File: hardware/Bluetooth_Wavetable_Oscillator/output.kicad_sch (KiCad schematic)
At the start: 14 parts, among them J2 AudioJack2, U6 NE5532

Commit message: add audio test files
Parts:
- C13, C14, C17, C18, C19: footprint (none) -> Capacitor_THT:C_Disc_D5.0mm_W2.5mm_P5.00mm
- C16: footprint (none) -> Capacitor_THT:CP_Radial_D5.0mm_P2.50mm
- R1, R2, R3, R4, R5: footprint (none) -> Resistor_THT:R_Axial_DIN0204_L3.6mm_D1.6mm_P7.62mm_Horizontal
- RV1: footprint (none) -> Trimmer-potentiometer:Trimmer-potentiometer
- U6: footprint (none) -> Package_DIP:DIP-8_W7.62mm
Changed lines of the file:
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@@
 			)
 		)
-		(property "Footprint" ""
+		(property "Footprint" "Resistor_THT:R_Axial_DIN0204_L3.6mm_D1.6mm_P7.62mm_Horizontal"
 			(at 168.91 99.568 90)
 			(effects
@@
 			)
 		)
-		(property "Footprint" ""
+		(property "Footprint" "Resistor_THT:R_Axial_DIN0204_L3.6mm_D1.6mm_P7.62mm_Horizontal"
 			(at 190.5 114.808 90)
 			(effects
@@
 			)
 		)
-		(property "Footprint" ""
+		(property "Footprint" "Capacitor_THT:CP_Radial_D5.0mm_P2.50mm"
 			(at 143.51 96.8248 0)
 			(effects
@@
 			)
 		)
-		(property "Footprint" ""
+		(property "Footprint" "Capacitor_THT:C_Disc_D5.0mm_W2.5mm_P5.00mm"
 			(at 159.7152 116.84 0)
 			(effects
@@
 			)
 		)
-		(property "Footprint" ""
+		(property "Footprint" "Resistor_THT:R_Axial_DIN0204_L3.6mm_D1.6mm_P7.62mm_Horizontal"
 			(at 78.74 97.028 90)
 			(effects
@@
 			)
 		)
-		(property "Footprint" ""
+		(property "Footprint" "Package_DIP:DIP-8_W7.62mm"
 			(at 189.23 99.06 0)
 			(effects
@@
 			)
 		)
-		(property "Footprint" ""
+		(property "Footprint" "Capacitor_THT:C_Disc_D5.0mm_W2.5mm_P5.00mm"
 			(at 104.14 83.5152 0)
 			(effects
@@
 			)
 		)
-		(property "Footprint" ""
+		(property "Footprint" "Package_DIP:DIP-8_W7.62mm"
 			(at 118.11 97.79 0)
 			(effects
@@
 			)
 		)
-		(property "Footprint" ""
+		(property "Footprint" "Capacitor_THT:C_Disc_D5.0mm_W2.5mm_P5.00mm"
 			(at 138.1252 179.07 0)
 			(effects
@@
 			)
 		)
-		(property "Footprint" ""
+		(property "Footprint" "Resistor_THT:R_Axial_DIN0204_L3.6mm_D1.6mm_P7.62mm_Horizontal"
 			(at 168.91 107.188 90)
 			(effects
@@
 			)
 		)
-		(property "Footprint" ""
+		(property "Footprint" "Package_DIP:DIP-8_W7.62mm"
 			(at 127 166.37 0)
 			(effects
@@
 			)
 		)
-		(property "Footprint" ""
+		(property "Footprint" "Capacitor_THT:C_Disc_D5.0mm_W2.5mm_P5.00mm"
 			(at 102.5652 106.68 0)
 			(effects
@@
 			)
 		)
-		(property "Footprint" ""
+		(property "Footprint" "Resistor_THT:R_Axial_DIN0204_L3.6mm_D1.6mm_P7.62mm_Horizontal"
 			(at 95.25 97.028 90)
 			(effects
@@
 			)
 		)
-		(property "Footprint" ""
+		(property "Footprint" "Trimmer-potentiometer:Trimmer-potentiometer"
 			(at 55.88 171.45 0)
 			(effects
@@
 			)
 		)
-		(property "Footprint" ""
+		(property "Footprint" "Capacitor_THT:C_Disc_D5.0mm_W2.5mm_P5.00mm"
 			(at 117.8052 179.07 0)
 			(effects

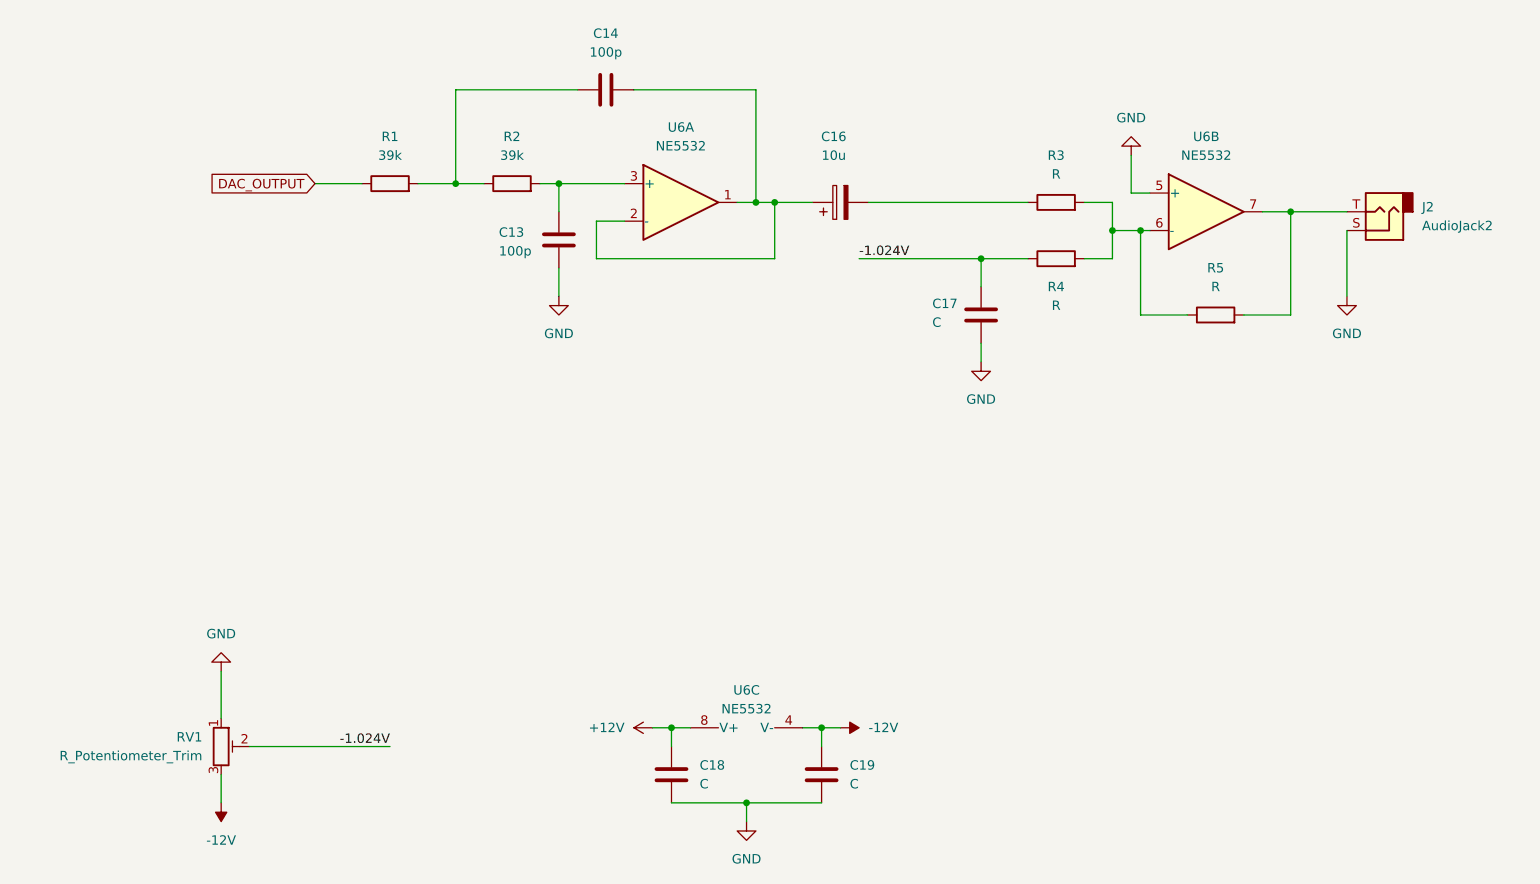
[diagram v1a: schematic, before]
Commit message: add bth components, add component values, update SPI pins, change disp power supply to 5V
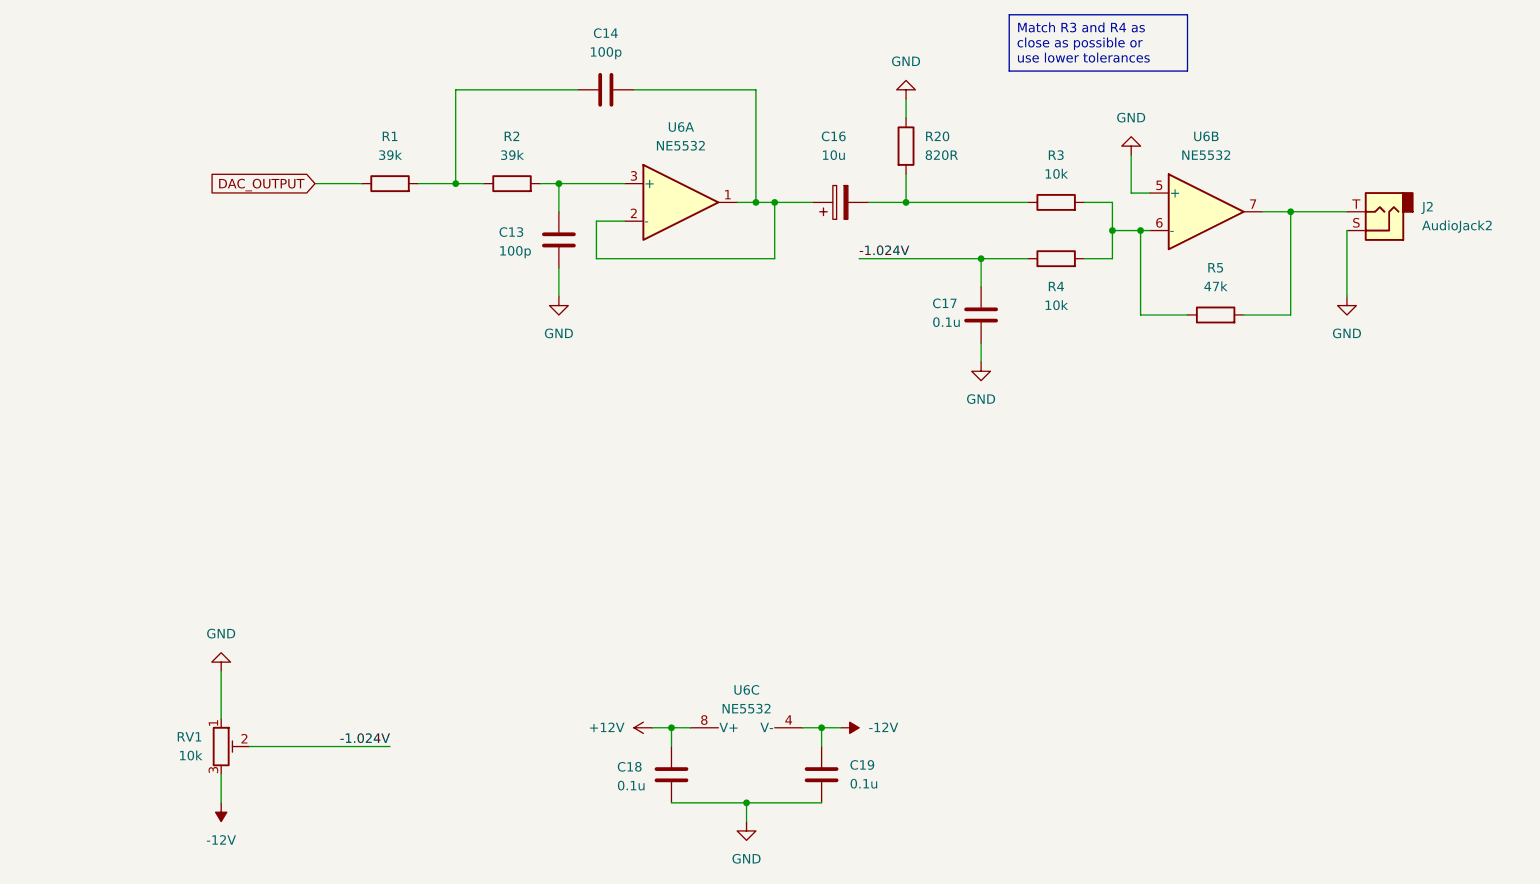
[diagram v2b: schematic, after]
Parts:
- added R20: 820R, symbol Device:R
- C17, C18, C19: value C -> 0.1u
- R3, R4: value R -> 10k
- R5: value R -> 47k
- RV1: value R_Potentiometer_Trim -> 10k
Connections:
- net GND: now also R20.1
- net at C16.2, R3.1: now also R20.2
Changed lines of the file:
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@@
+	)
+	(junction
+		(at 148.59 97.79)
+		(diameter 0)
+		(color 0 0 0 0)
 	)
 	(junction
@@
 	(wire
 		(pts
+			(xy 148.59 93.98) (xy 148.59 97.79)
+		)
+		(stroke
+			(width 0)
+			(type default)
+		)
+	)
+	(wire
+		(pts
 			(xy 142.24 105.41) (xy 158.75 105.41)
 		)
@@
 	(wire
 		(pts
-			(xy 143.51 97.79) (xy 165.1 97.79)
+			(xy 143.51 97.79) (xy 148.59 97.79)
 		)
 		(stroke
@@
 	(wire
 		(pts
+			(xy 148.59 83.82) (xy 148.59 86.36)
+		)
+		(stroke
+			(width 0)
+			(type default)
+		)
+	)
+	(wire
+		(pts
 			(xy 128.27 97.79) (xy 125.73 97.79)
 		)
@@
 	(wire
 		(pts
+			(xy 148.59 97.79) (xy 165.1 97.79)
+		)
+		(stroke
+			(width 0)
+			(type default)
+		)
+	)
+	(wire
+		(pts
 			(xy 130.81 97.79) (xy 128.27 97.79)
 		)
@@
 		)
 	)
-	(label "-1.024V"
-		(at 142.24 105.41 0)
-		(fields_autoplaced yes)
+	(text_box "Match R3 and R4 as close as possible or use lower tolerances"
+		(exclude_from_sim no)
+		(at 162.56 72.39 0)
+		(size 24.13 7.62)
+		(stroke
+			(width 0)
+			(type default)
+		)
+		(fill
+			(type none)
+		)
 		(effects
 			(font
 				(size 1.27 1.27)
 			)
-			(justify left bottom)
+			(justify left top)
 		)
 	)
 	(label "-1.024V"
-		(at 78.74 171.45 180)
+		(at 142.24 105.41 0)
 		(fields_autoplaced yes)
 		(effects
@@
 				(size 1.27 1.27)
 			)
+			(justify left bottom)
+		)
+	)
+	(label "-1.024V"
+		(at 78.74 171.45 180)
+		(fields_autoplaced yes)
+		(effects
+			(font
+				(size 1.27 1.27)
+			)
 			(justify right bottom)
 		)
@@
 			)
 		)
-		(property "Value" "R"
+		(property "Value" "10k"
 			(at 168.91 93.98 90)
 			(effects
@@
 	)
 	(symbol
+		(lib_id "power:GND")
+		(at 148.59 83.82 180)
+		(unit 1)
+		(exclude_from_sim no)
+		(in_bom yes)
+		(on_board yes)
+		(dnp no)
+		(fields_autoplaced yes)
+		(property "Reference" "#PWR051"
+			(at 148.59 77.47 0)
+			(effects
+				(font
+					(size 1.27 1.27)
+				)
+				(hide yes)
+			)
+		)
+		(property "Value" "GND"
+			(at 148.59 78.74 0)
+			(effects
+				(font
+					(size 1.27 1.27)
+				)
+			)
+		)
+		(property "Footprint" ""
+			(at 148.59 83.82 0)
+			(effects
+				(font
+					(size 1.27 1.27)
+				)
+				(hide yes)
+			)
+		)
+		(property "Datasheet" ""
+			(at 148.59 83.82 0)
+			(effects
+				(font
+					(size 1.27 1.27)
+				)
+				(hide yes)
+			)
+		)
+		(property "Description" "Power symbol creates a global label with name \"GND\" , ground"
+			(at 148.59 83.82 0)
+			(effects
+				(font
+					(size 1.27 1.27)
+				)
+				(hide yes)
+			)
+		)
+		(pin "1"
+		)
+		(instances
+			(project ""
+				(path "/fda99055-d953-4203-b673-64a5e6540552/e721cc72-9f0b-4653-9ded-ede3b48f082c"
+					(reference "#PWR051")
+					(unit 1)
+				)
+			)
+		)
+	)
+	(symbol
 		(lib_id "Device:R")
 		(at 190.5 113.03 90)
@@
 			)
 		)
-		(property "Value" "R"
+		(property "Value" "47k"
 			(at 190.5 109.22 90)
 			(effects
@@
 			)
 		)
-		(property "Value" "C"
+		(property "Value" "0.1u"
 			(at 152.146 114.046 0)
 			(effects
@@
 	)
 	(symbol
+		(lib_id "Device:R")
+		(at 148.59 90.17 0)
+		(unit 1)
+		(exclude_from_sim no)
+		(in_bom yes)
+		(on_board yes)
+		(dnp no)
+		(fields_autoplaced yes)
+		(property "Reference" "R20"
+			(at 151.13 88.8999 0)
+			(effects
+				(font
+					(size 1.27 1.27)
+				)
+				(justify left)
+			)
+		)
+		(property "Value" "820R"
+			(at 151.13 91.4399 0)
+			(effects
+				(font
+					(size 1.27 1.27)
+				)
+				(justify left)
+			)
+		)
+		(property "Footprint" ""
+			(at 146.812 90.17 90)
+			(effects
+				(font
+					(size 1.27 1.27)
+				)
+				(hide yes)
+			)
+		)
+		(property "Datasheet" "~"
+			(at 148.59 90.17 0)
+			(effects
+				(font
+					(size 1.27 1.27)
+				)
+				(hide yes)
+			)
+		)
+		(property "Description" "Resistor"
+			(at 148.59 90.17 0)
+			(effects
+				(font
+					(size 1.27 1.27)
+				)
+				(hide yes)
+			)
+		)
+		(pin "1"
+		)
+		(pin "2"
+		)
+		(instances
+			(project ""
+				(path "/fda99055-d953-4203-b673-64a5e6540552/e721cc72-9f0b-4653-9ded-ede3b48f082c"
+					(reference "R20")
+					(unit 1)
+				)
+			)
+		)
+	)
+	(symbol
 		(lib_id "Device:C")
 		(at 107.95 82.55 270)
@@
 			)
 		)
-		(property "Value" "C"
+		(property "Value" "0.1u"
 			(at 140.97 176.5299 0)
 			(effects
@@
 			)
 		)
-		(property "Value" "R"
+		(property "Value" "10k"
 			(at 168.91 111.76 90)
 			(effects
@@
 			)
 		)
-		(property "Value" "R_Potentiometer_Trim"
+		(property "Value" "10k"
 			(at 53.34 172.7199 0)
 			(effects
@@
 		(on_board yes)
 		(dnp no)
-		(fields_autoplaced yes)
 		(property "Reference" "C18"
-			(at 120.65 173.9899 0)
+			(at 109.474 174.244 0)
 			(effects
 				(font
@@
 			)
 		)
-		(property "Value" "C"
-			(at 120.65 176.5299 0)
-			(effects
-				(font
+		(property "Value" "0.1u"
+			(at 109.474 176.784 0)
+			(effects
+				(font

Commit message: start PCB layout
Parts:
- J2: footprint (none) -> Connector_Audio:Jack_3.5mm_QingPu_WQP-PJ398SM_Vertical_CircularHoles
- R1, R2, R3, R4, R5: footprint Resistor_THT:R_Axial_DIN0204_L3.6mm_D1.6mm_P7.62mm_Horizontal -> Resistor_THT:R_Axial_DIN0204_L3.6mm_D1.6mm_P2.54mm_Vertical
- R20: footprint (none) -> Resistor_THT:R_Axial_DIN0204_L3.6mm_D1.6mm_P2.54mm_Vertical
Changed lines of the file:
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@@
 			)
 		)
-		(property "Footprint" "Resistor_THT:R_Axial_DIN0204_L3.6mm_D1.6mm_P7.62mm_Horizontal"
+		(property "Footprint" "Resistor_THT:R_Axial_DIN0204_L3.6mm_D1.6mm_P2.54mm_Vertical"
 			(at 168.91 99.568 90)
 			(effects
@@
 			)
 		)
-		(property "Footprint" "Resistor_THT:R_Axial_DIN0204_L3.6mm_D1.6mm_P7.62mm_Horizontal"
+		(property "Footprint" "Resistor_THT:R_Axial_DIN0204_L3.6mm_D1.6mm_P2.54mm_Vertical"
 			(at 190.5 114.808 90)
 			(effects
@@
 			)
 		)
-		(property "Footprint" "Resistor_THT:R_Axial_DIN0204_L3.6mm_D1.6mm_P7.62mm_Horizontal"
+		(property "Footprint" "Resistor_THT:R_Axial_DIN0204_L3.6mm_D1.6mm_P2.54mm_Vertical"
 			(at 78.74 97.028 90)
 			(effects
@@
 			)
 		)
-		(property "Footprint" ""
+		(property "Footprint" "Resistor_THT:R_Axial_DIN0204_L3.6mm_D1.6mm_P2.54mm_Vertical"
 			(at 146.812 90.17 90)
 			(effects
@@
 			)
 		)
-		(property "Footprint" "Resistor_THT:R_Axial_DIN0204_L3.6mm_D1.6mm_P7.62mm_Horizontal"
+		(property "Footprint" "Resistor_THT:R_Axial_DIN0204_L3.6mm_D1.6mm_P2.54mm_Vertical"
 			(at 168.91 107.188 90)
 			(effects
@@
 			)
 		)
-		(property "Footprint" ""
+		(property "Footprint" "Connector_Audio:Jack_3.5mm_QingPu_WQP-PJ398SM_Vertical_CircularHoles"
 			(at 213.36 99.06 0)
 			(effects
@@
 			)
 		)
-		(property "Footprint" "Resistor_THT:R_Axial_DIN0204_L3.6mm_D1.6mm_P7.62mm_Horizontal"
+		(property "Footprint" "Resistor_THT:R_Axial_DIN0204_L3.6mm_D1.6mm_P2.54mm_Vertical"
 			(at 95.25 97.028 90)
 			(effects

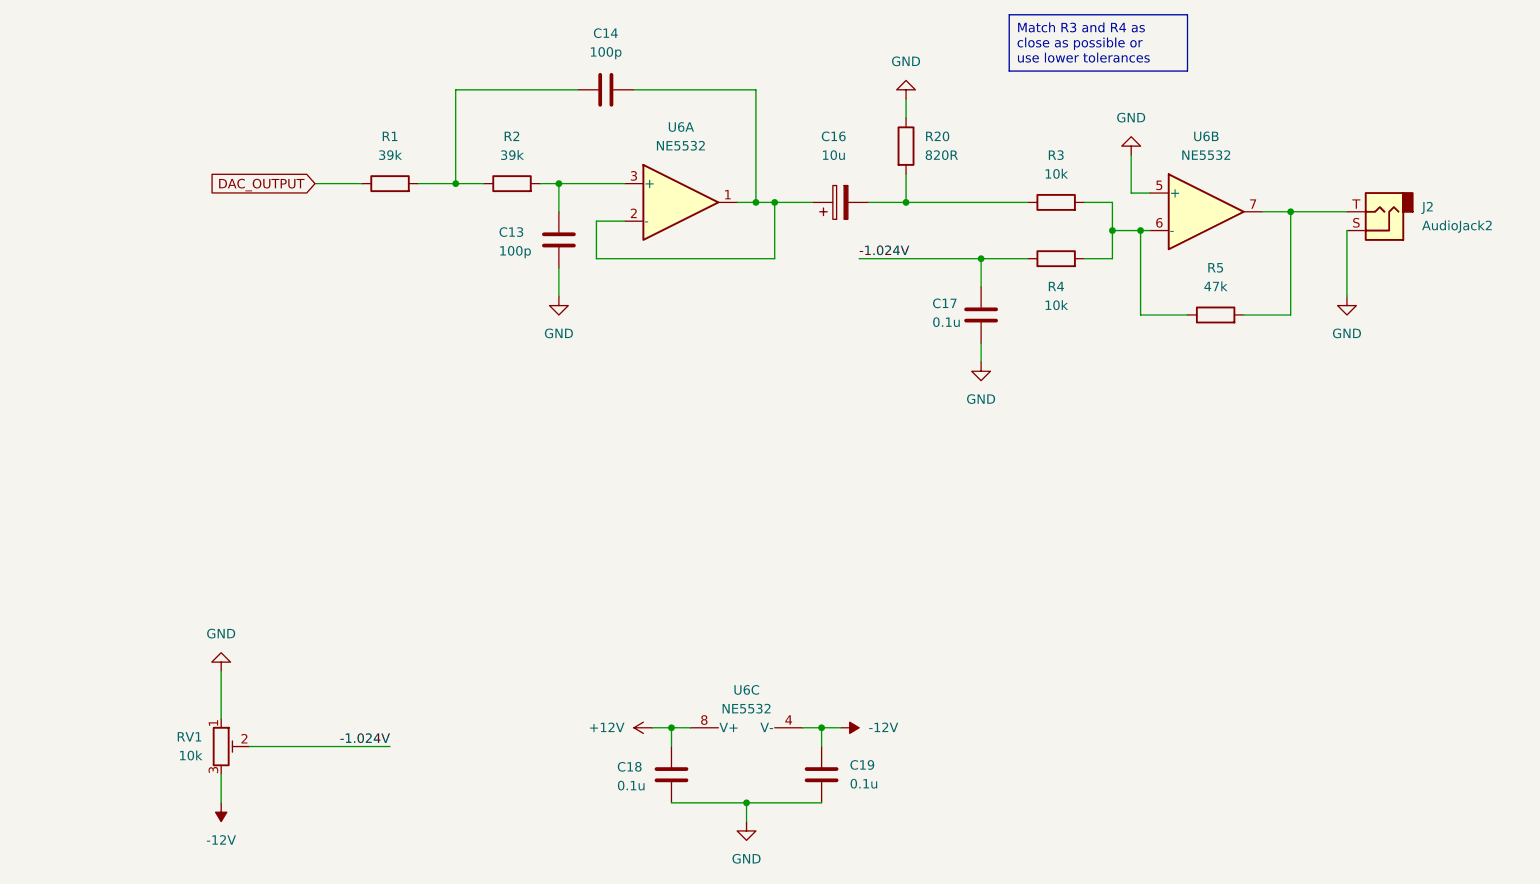
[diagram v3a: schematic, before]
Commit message: update shematic, PCB and footprints
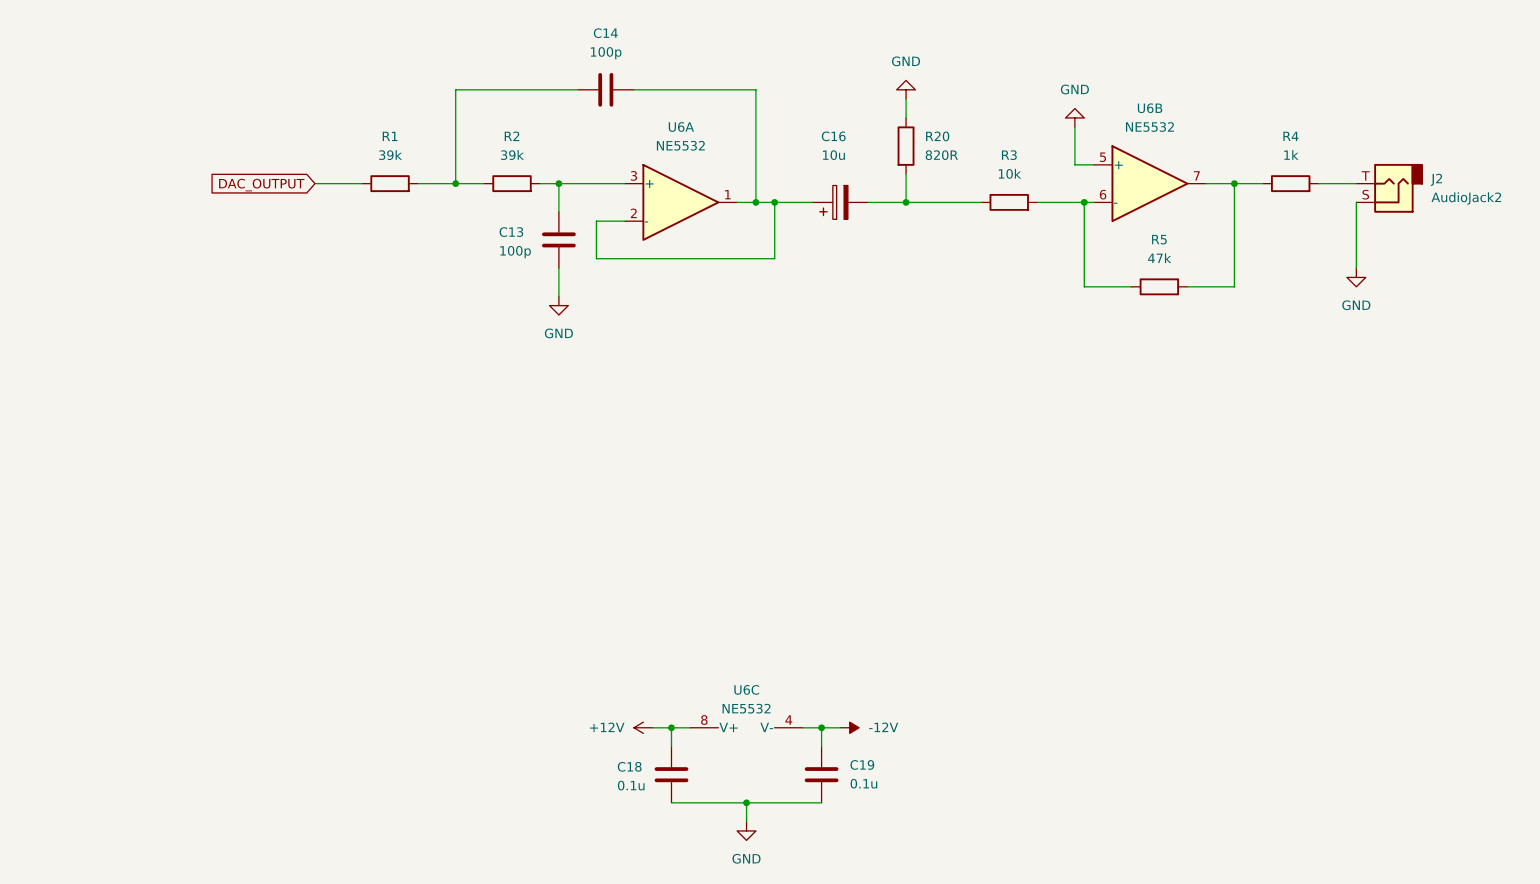
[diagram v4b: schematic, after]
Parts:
- removed C17: 0.1u, Capacitor_THT:C_Disc_D5.0mm_W2.5mm_P5.00mm, symbol Device:C
- removed RV1: 10k, Trimmer-potentiometer:Trimmer-potentiometer, symbol Device:R_Potentiometer_Trim
- R4: value 10k -> 1k
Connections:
- net -1.024V is gone; now on an unnamed net: R4.1
- net at R3.2, R5.1, U6.6 (-): no longer R4.2
- net at R5.2, U6.7: no longer J2.T
- new net: J2.T, R4.2
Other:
- moved on the sheet: J2, R3, R5, U6B

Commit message: all items connected
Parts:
- R1, R2, R20, R3, R4, R5: footprint Resistor_THT:R_Axial_DIN0204_L3.6mm_D1.6mm_P2.54mm_Vertical -> Resistor_THT:R_Axial_DIN0204_L3.6mm_D1.6mm_P7.62mm_Horizontal
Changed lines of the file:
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@@
 			)
 		)
-		(property "Footprint" "Resistor_THT:R_Axial_DIN0204_L3.6mm_D1.6mm_P2.54mm_Vertical"
+		(property "Footprint" "Resistor_THT:R_Axial_DIN0204_L3.6mm_D1.6mm_P7.62mm_Horizontal"
 			(at 162.56 99.568 90)
 			(effects
@@
 			)
 		)
-		(property "Footprint" "Resistor_THT:R_Axial_DIN0204_L3.6mm_D1.6mm_P2.54mm_Vertical"
+		(property "Footprint" "Resistor_THT:R_Axial_DIN0204_L3.6mm_D1.6mm_P7.62mm_Horizontal"
 			(at 182.88 110.998 90)
 			(effects
@@
 			)
 		)
-		(property "Footprint" "Resistor_THT:R_Axial_DIN0204_L3.6mm_D1.6mm_P2.54mm_Vertical"
+		(property "Footprint" "Resistor_THT:R_Axial_DIN0204_L3.6mm_D1.6mm_P7.62mm_Horizontal"
 			(at 78.74 97.028 90)
 			(effects
@@
 			)
 		)
-		(property "Footprint" "Resistor_THT:R_Axial_DIN0204_L3.6mm_D1.6mm_P2.54mm_Vertical"
+		(property "Footprint" "Resistor_THT:R_Axial_DIN0204_L3.6mm_D1.6mm_P7.62mm_Horizontal"
 			(at 146.812 90.17 90)
 			(effects
@@
 			)
 		)
-		(property "Footprint" "Resistor_THT:R_Axial_DIN0204_L3.6mm_D1.6mm_P2.54mm_Vertical"
+		(property "Footprint" "Resistor_THT:R_Axial_DIN0204_L3.6mm_D1.6mm_P7.62mm_Horizontal"
 			(at 200.66 97.028 90)
 			(effects
@@
 			)
 		)
-		(property "Footprint" "Resistor_THT:R_Axial_DIN0204_L3.6mm_D1.6mm_P2.54mm_Vertical"
+		(property "Footprint" "Resistor_THT:R_Axial_DIN0204_L3.6mm_D1.6mm_P7.62mm_Horizontal"
 			(at 95.25 97.028 90)
 			(effects
